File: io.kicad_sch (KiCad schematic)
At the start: 21 parts, among them J30 FTDI-MCU, J31 UART-DALI, J40 A10-0, J41 A5-0, J42 A5-5, J43 A2-0, J44 A2-2, J45 A2-4, J46 A2-6, J47 A2-8, J50 D8-11, J51 D4-11, J52 D4-16, J53 D2-11, J54 D2-13, J55 D2-16, J56 D2-18, J60 D1-11, J61 D1-12, J62 D1-13, J63 D1-14

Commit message: Remove the kitchen sink
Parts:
- removed J30: FTDI-MCU, Connector_PinHeader_2.54mm:PinHeader_1x06_P2.54mm_Vertical, symbol Connector:Conn_01x06_Pin
- removed J41: A5-0, Connector_PinHeader_2.54mm:PinHeader_1x08_P2.54mm_Vertical, symbol Connector:Conn_01x08_Pin
- removed J42: A5-5, Connector_PinHeader_2.54mm:PinHeader_1x08_P2.54mm_Vertical, symbol Connector:Conn_01x08_Pin
- removed J43: A2-0, Connector_PinHeader_2.54mm:PinHeader_1x05_P2.54mm_Vertical, symbol Connector:Conn_01x05_Pin
- removed J44: A2-2, Connector_PinHeader_2.54mm:PinHeader_1x05_P2.54mm_Vertical, symbol Connector:Conn_01x05_Pin
- removed J45: A2-4, Connector_PinHeader_2.54mm:PinHeader_1x05_P2.54mm_Vertical, symbol Connector:Conn_01x05_Pin
- removed J46: A2-6, Connector_PinHeader_2.54mm:PinHeader_1x05_P2.54mm_Vertical, symbol Connector:Conn_01x05_Pin
- removed J47: A2-8, Connector_PinHeader_2.54mm:PinHeader_1x05_P2.54mm_Vertical, symbol Connector:Conn_01x05_Pin
- removed J51: D4-11, Connector_PinHeader_2.54mm:PinHeader_1x07_P2.54mm_Vertical, symbol Connector:Conn_01x07_Pin
- removed J52: D4-16, Connector_PinHeader_2.54mm:PinHeader_1x07_P2.54mm_Vertical, symbol Connector:Conn_01x07_Pin
- removed J53: D2-11, Connector_PinHeader_2.54mm:PinHeader_1x05_P2.54mm_Vertical, symbol Connector:Conn_01x05_Pin
- removed J54: D2-13, Connector_PinHeader_2.54mm:PinHeader_1x05_P2.54mm_Vertical, symbol Connector:Conn_01x05_Pin
- removed J55: D2-16, Connector_PinHeader_2.54mm:PinHeader_1x05_P2.54mm_Vertical, symbol Connector:Conn_01x05_Pin
- removed J56: D2-18, Connector_PinHeader_2.54mm:PinHeader_1x05_P2.54mm_Vertical, symbol Connector:Conn_01x05_Pin
- removed J60: D1-11, Connector_PinHeader_2.54mm:PinHeader_1x02_P2.54mm_Vertical, symbol Connector:Conn_01x02_Pin
- removed J61: D1-12, Connector_PinHeader_2.54mm:PinHeader_1x02_P2.54mm_Vertical, symbol Connector:Conn_01x02_Pin
- removed J62: D1-13, Connector_PinHeader_2.54mm:PinHeader_1x02_P2.54mm_Vertical, symbol Connector:Conn_01x02_Pin
- removed J63: D1-14, Connector_PinHeader_2.54mm:PinHeader_1x02_P2.54mm_Vertical, symbol Connector:Conn_01x02_Pin
- J7: renamed from J31; value UART-DALI -> UART
- J8: renamed from J40; footprint Connector_PinHeader_2.54mm:PinHeader_1x13_P2.54mm_Vertical -> Connector_PinHeader_2.54mm:PinHeader_2x13_P2.54mm_Vertical; symbol Connector:Conn_01x13_Pin -> Connector_Generic:Conn_02x13_Odd_Even
- J9: renamed from J50; footprint Connector_PinHeader_2.54mm:PinHeader_1x11_P2.54mm_Vertical -> Connector_PinHeader_2.54mm:PinHeader_2x13_P2.54mm_Vertical; symbol Connector:Conn_01x11_Pin -> Connector_Generic:Conn_02x13_Odd_Even
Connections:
- net +3.3V: now also J8.3 (Pin_3), J8.4 (Pin_4), J9.3 (Pin_3), J9.4 (Pin_4); no longer J8.2 (Pin_2), J9.2 (Pin_2)
- net +5V: now also J8.2 (Pin_2), J9.2 (Pin_2)
- net GND: now also J8.10 (Pin_10), J8.12 (Pin_12), J8.14 (Pin_14), J8.16 (Pin_16), J8.18 (Pin_18), J8.20 (Pin_20), J8.22 (Pin_22), J8.24 (Pin_24), J8.26 (Pin_26), J8.5 (Pin_5), J8.6 (Pin_6), J8.8 (Pin_8), J9.11 (Pin_11), J9.13 (Pin_13), J9.15 (Pin_15), J9.17 (Pin_17), J9.19 (Pin_19), J9.21 (Pin_21), J9.23 (Pin_23), J9.25 (Pin_25), J9.5 (Pin_5), J9.6 (Pin_6), J9.7 (Pin_7), J9.9 (Pin_9); no longer J8.3 (Pin_3), J9.3 (Pin_3)
- net IO_A0: now also J8.7 (Pin_7); no longer J8.4 (Pin_4)
- net IO_A1: now also J8.9 (Pin_9); no longer J8.5 (Pin_5)
- net IO_A2: now also J8.11 (Pin_11); no longer J8.6 (Pin_6)
- net IO_A3: now also J8.13 (Pin_13); no longer J8.7 (Pin_7)
- net IO_A4: now also J8.15 (Pin_15); no longer J8.8 (Pin_8)
- net IO_A5: now also J8.17 (Pin_17); no longer J8.9 (Pin_9)
- net IO_A6: now also J8.19 (Pin_19); no longer J8.10 (Pin_10)
- net IO_A7: now also J8.21 (Pin_21); no longer J8.11 (Pin_11)
- net IO_A8: now also J8.23 (Pin_23); no longer J8.12 (Pin_12)
- net IO_A9: now also J8.25 (Pin_25); no longer J8.13 (Pin_13)
- net IO_D11: now also J9.8 (Pin_8); no longer J9.4 (Pin_4)
- net IO_D12: now also J9.10 (Pin_10); no longer J9.5 (Pin_5)
- net IO_D13: now also J9.12 (Pin_12); no longer J9.6 (Pin_6)
- net IO_D14: now also J9.14 (Pin_14); no longer J9.7 (Pin_7)
- net IO_D16: now also J9.16 (Pin_16); no longer J9.8 (Pin_8)
- net IO_D17: now also J9.18 (Pin_18); no longer J9.9 (Pin_9)
- net IO_D18: now also J9.20 (Pin_20); no longer J9.10 (Pin_10)
- net IO_D39: now also J9.22 (Pin_22); no longer J9.11 (Pin_11)
- new net IO_D41: J9.24 (Pin_24)
- new net IO_D42: J9.26 (Pin_26)
- no-connect marks 3 -> 0
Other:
- moved on the sheet: J7

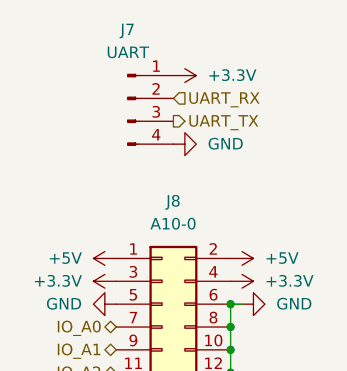
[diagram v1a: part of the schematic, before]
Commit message: Rename the UART connection to DIRECT because it needs Manchester encoding
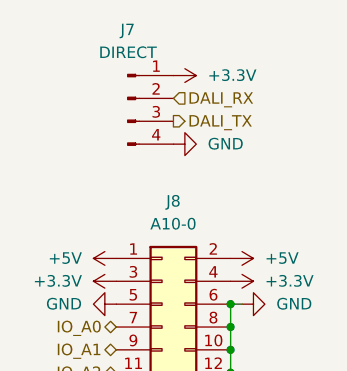
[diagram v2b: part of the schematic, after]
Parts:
- J7: value UART -> DIRECT
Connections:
- net UART_RX renamed DALI_RX
- net UART_TX renamed DALI_TX
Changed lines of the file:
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@@
 		)
 	)
-	(hierarchical_label "UART_RX"
+	(hierarchical_label "DALI_RX"
 		(shape input)
 		(at 20.32 12.7 0)
@@
 		)
 	)
-	(hierarchical_label "UART_TX"
+	(hierarchical_label "DALI_TX"
 		(shape output)
 		(at 20.32 15.24 0)
@@
 			)
 		)
-		(property "Value" "UART"
+		(property "Value" "DIRECT"
 			(at 15.24 7.62 0)
 			(effects

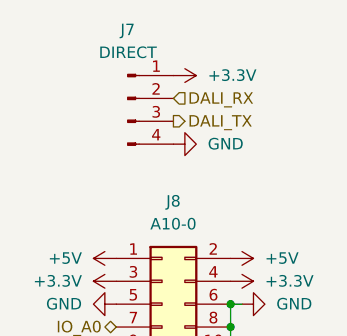
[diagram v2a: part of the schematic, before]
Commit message: Avoid using the name "DIRECT" in two places with different meanings
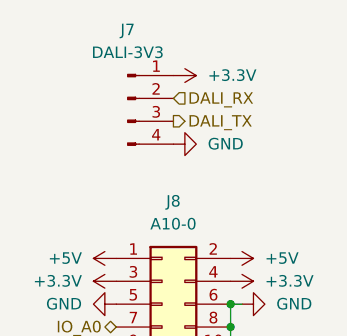
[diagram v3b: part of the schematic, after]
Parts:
- J7: value DIRECT -> DALI-3V3
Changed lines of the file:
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@@
 			)
 		)
-		(property "Value" "DIRECT"
+		(property "Value" "DALI-3V3"
 			(at 15.24 7.62 0)
 			(effects
